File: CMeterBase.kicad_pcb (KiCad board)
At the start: 2 copper layers, 74.4 x 103.6 mm, 24 parts, among them J1 Screw_Terminal_01x02, J2 PCB_CONN, Q1 Q_NPN_ECB, T1 L_Measure, T2 TPK-1-6

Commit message: update
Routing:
- net +5V: track 165.6 -> 165.1 mm
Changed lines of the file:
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@@
     (thickness 1.6)
     (drawings 5)
-    (tracks 85)
+    (tracks 83)
     (zones 0)
     (modules 24)
@@
   )
   (setup
-    (last_trace_width 1)
+    (last_trace_width 0.5)
     (user_trace_width 0.5)
     (user_trace_width 0.8)
@@
     (visible_elements 7FFFFF7F)
     (pcbplotparams
-      (layerselection 0x00030_80000001)
+      (layerselection 0x010f0_80000001)
       (usegerberextensions false)
       (excludeedgelayer true)
@@
       (outputformat 1)
       (mirror false)
-      (drillshape 1)
+      (drillshape 0)
       (scaleselection 1)
-      (outputdirectory ""))
+      (outputdirectory GerberBase))
   )
   (net 0 "")
@@
       (effects (font (size 1 1) (thickness 0.15)))
     )
-    (fp_text value TL431 (at -1.7 -4.5 180) (layer F.Fab)
-      (effects (font (size 1 1) (thickness 0.15)))
-    )
-    (fp_text user TL431 (at -1.7 -4.5 180) (layer F.SilkS)
+    (fp_text value TL431 (at -1.75 -4.65 180) (layer F.Fab)
+      (effects (font (size 1 1) (thickness 0.15)))
+    )
+    (fp_text user TL431 (at -1.75 -4.65 180) (layer F.SilkS)
       (effects (font (size 1 1) (thickness 0.15)))
     )
@@
   (segment (start 86.22 96.49) (end 86.22 98.68) (width 1) (layer F.Cu) (net 2))
   (segment (start 86.22 98.68) (end 84.6 100.3) (width 1) (layer F.Cu) (net 2))
-  (segment (start 127.4 119.4) (end 127.58 119.58) (width 1) (layer F.Cu) (net 3))
   (segment (start 127.4 119.4) (end 127.4 115.47) (width 1) (layer F.Cu) (net 3))
   (segment (start 127.58 119.58) (end 131 119.58) (width 1) (layer F.Cu) (net 3))
@@
   (segment (start 71 62) (end 65.3 62) (width 1) (layer F.Cu) (net 4))
   (segment (start 72.05 70.35) (end 74.05 68.35) (width 1) (layer F.Cu) (net 4))
-  (segment (start 73.3 62) (end 71 62) (width 1) (layer F.Cu) (net 4))
-  (segment (start 74.05 62.75) (end 73.3 62) (width 1) (layer F.Cu) (net 4))
-  (segment (start 74.05 68.35) (end 74.05 62.75) (width 1) (layer F.Cu) (net 4))
+  (segment (start 73 62) (end 71 62) (width 1) (layer F.Cu) (net 4))
+  (segment (start 74.05 63.05) (end 73 62) (width 1) (layer F.Cu) (net 4))
+  (segment (start 74.05 68.35) (end 74.05 63.05) (width 1) (layer F.Cu) (net 4))
   (segment (start 75.4 81.65) (end 74.1 80.35) (width 1) (layer F.Cu) (net 4))
   (segment (start 75.4 95.1) (end 75.4 81.65) (width 1) (layer F.Cu) (net 4))
@@
   (segment (start 72.05 73.65) (end 72.05 70.35) (width 1) (layer F.Cu) (net 4))
   (segment (start 89.7 100.4) (end 89.7 94.5) (width 1) (layer F.Cu) (net 4))
-  (segment (start 82.6 117.7) (end 81.9 117) (width 1) (layer F.Cu) (net 4))
-  (segment (start 81.9 117) (end 81.9 108.2) (width 1) (layer F.Cu) (net 4))
+  (segment (start 82.9 117.7) (end 81.9 116.7) (width 1) (layer F.Cu) (net 4))
+  (segment (start 81.9 116.7) (end 81.9 108.2) (width 1) (layer F.Cu) (net 4))
   (segment (start 81.9 108.2) (end 89.7 100.4) (width 1) (layer F.Cu) (net 4))
-  (segment (start 84.4 117.7) (end 82.6 117.7) (width 1) (layer F.Cu) (net 4))
-  (segment (start 89.7 94.5) (end 89.5 94.5) (width 1) (layer F.Cu) (net 4))
+  (segment (start 84.4 117.7) (end 82.9 117.7) (width 1) (layer F.Cu) (net 4))
   (segment (start 85.75 89.3) (end 85.75 93) (width 1) (layer F.Cu) (net 4))
   (segment (start 103.75 94.5) (end 89.5 94.5) (width 1) (layer F.Cu) (net 4))
@@
   (segment (start 65.15 76.55) (end 68.15 73.55) (width 1) (layer F.Cu) (net 11))
   (segment (start 65.15 82.73) (end 65.15 76.55) (width 1) (layer F.Cu) (net 11))
-  (segment (start 68.96 64.54) (end 71 64.54) (width 1) (layer F.Cu) (net 11))
-  (segment (start 68.15 65.35) (end 68.96 64.54) (width 1) (layer F.Cu) (net 11))
-  (segment (start 68.15 73.55) (end 68.15 65.35) (width 1) (layer F.Cu) (net 11))
+  (segment (start 69.21 64.54) (end 71 64.54) (width 1) (layer F.Cu) (net 11))
+  (segment (start 68.15 65.6) (end 69.21 64.54) (width 1) (layer F.Cu) (net 11))
+  (segment (start 68.15 73.55) (end 68.15 65.6) (width 1) (layer F.Cu) (net 11))
   (segment (start 67.49 96.49) (end 63.95 92.95) (width 1) (layer F.Cu) (net 11))
   (segment (start 70.98 96.49) (end 67.49 96.49) (width 1) (layer F.Cu) (net 11))

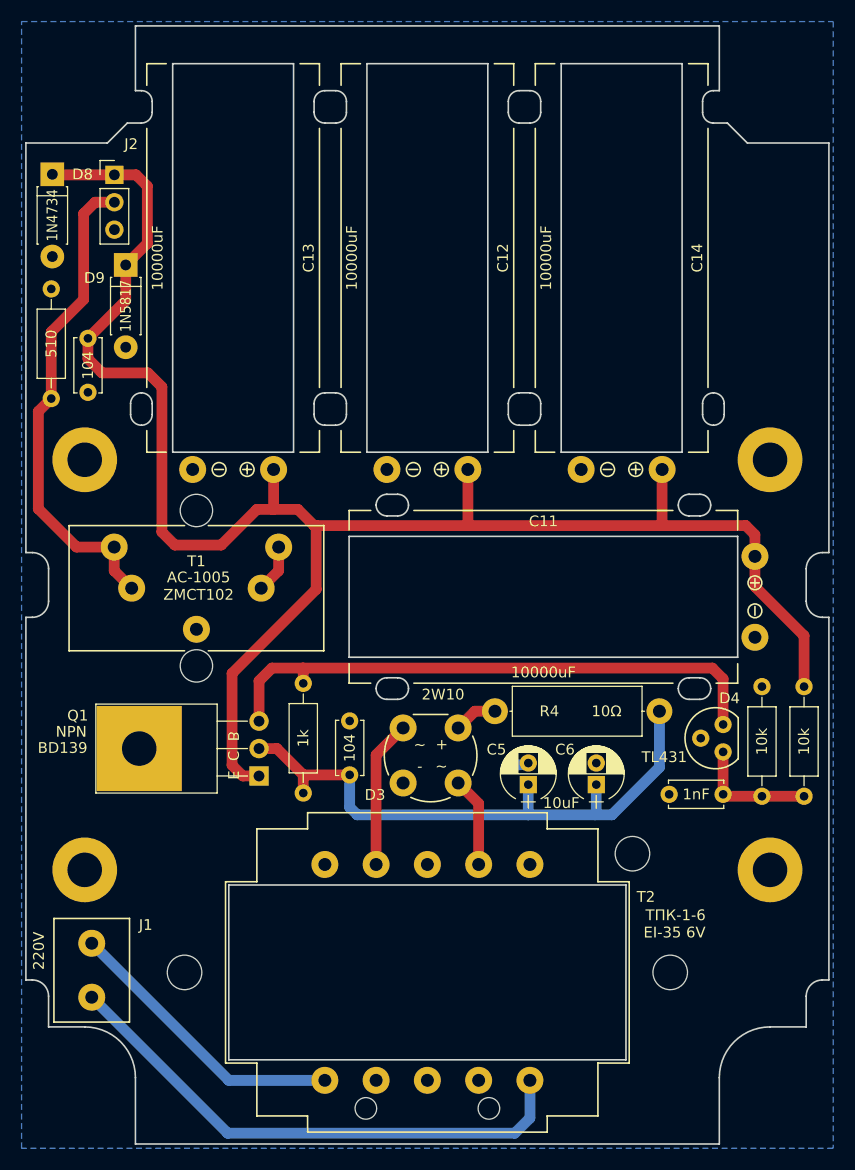
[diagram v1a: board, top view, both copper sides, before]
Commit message: internal milling areas changed for jlcpcb
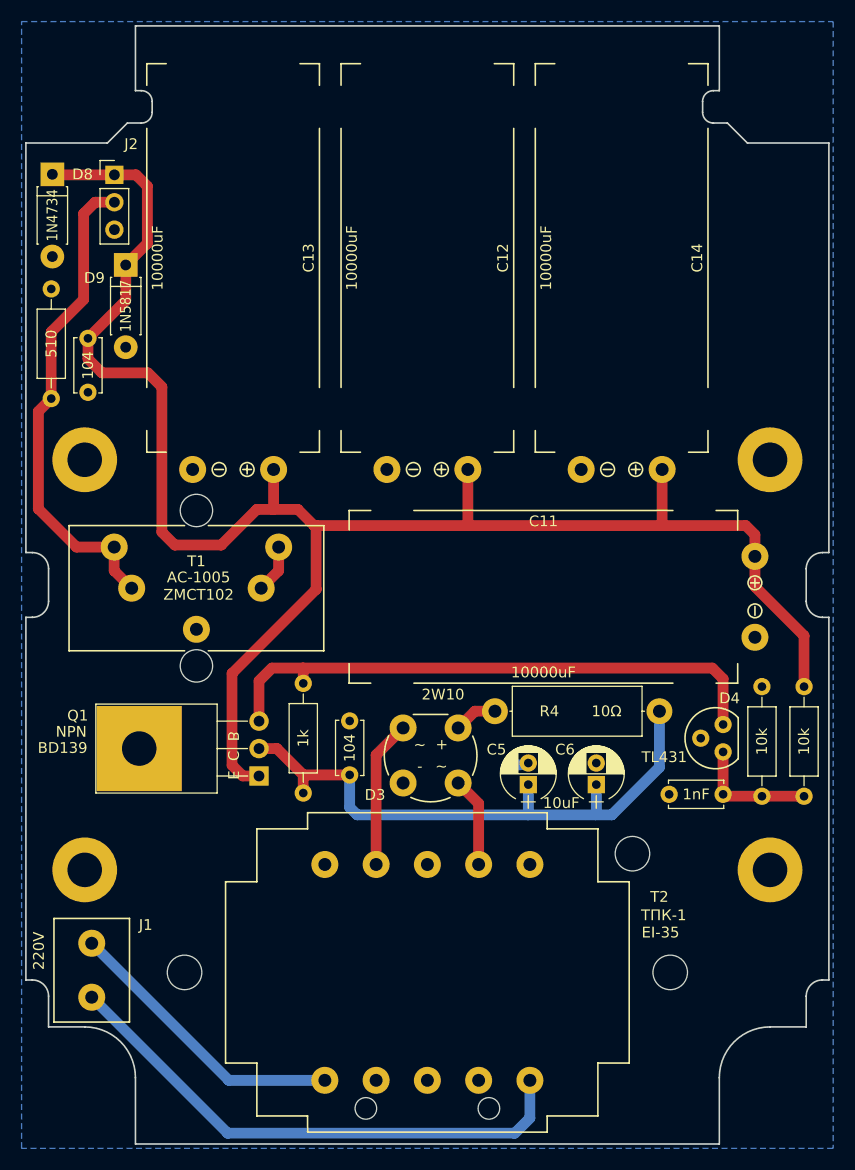
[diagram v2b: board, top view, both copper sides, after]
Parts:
- C12, C13, C14: footprint MyFootprints:CAP_D16_L36-2 -> MyFootprints:CAP_D16_L36-4
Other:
- outline, holes or cut-outs redrawn
